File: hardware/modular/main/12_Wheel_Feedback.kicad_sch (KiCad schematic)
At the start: 6 parts, among them J6 ENCODER_8P, U28 TPS22919DCKR

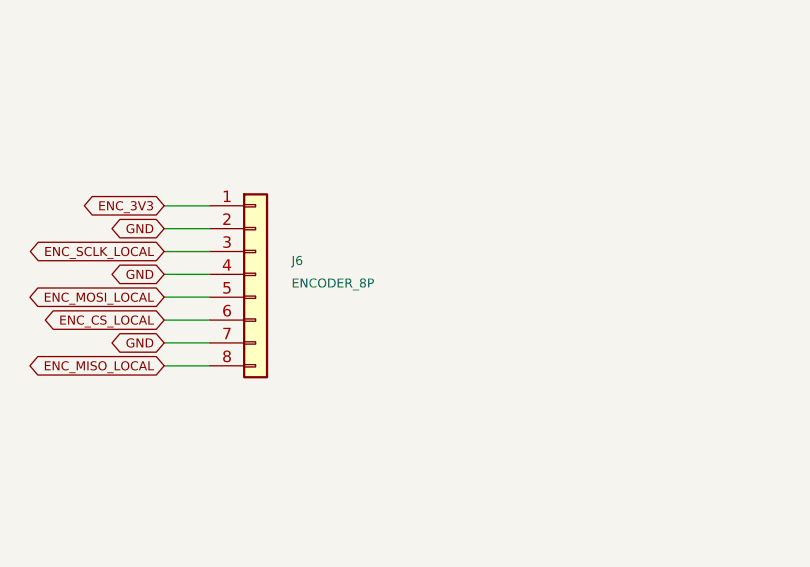
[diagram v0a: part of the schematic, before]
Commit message: Prepare wired Rev-A bench boards and submit manufacturing review
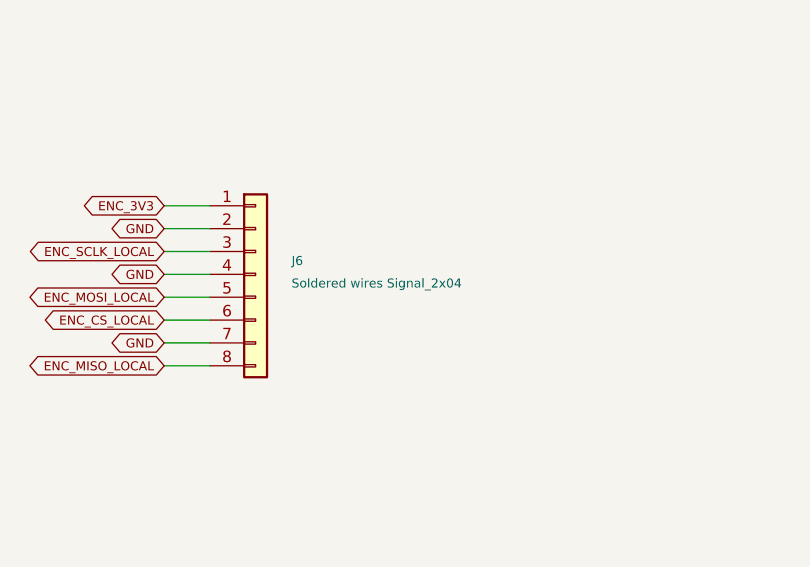
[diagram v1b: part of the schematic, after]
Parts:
- J6: value ENCODER_8P -> Soldered wires Signal_2x04; footprint Connector_JST:JST_SH_SM08B-SRSS-TB_1x08-1MP_P1.00mm_Horizontal -> MagMouseModular:Wire_Signal_2x04_P2.54mm; JLCPCB Part # C160407 -> (none); LCSC C160407 -> (none); MPN SM08B-SRSS-TB(LF)(SN) -> (none); Manufacturer JST -> (none); Sourcing Status JLCPCB SMT listing checked 2026-09-09; order stock and harn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 -> Hand-soldered wire termination; no connector fitted; do not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; Supplier URL https://www.lcsc.com/product-detail/C160407.html -> (none)
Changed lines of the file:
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@@
           (size 1.0 1.0))
         (justify left)))
-    (property "Value" "ENCODER_8P"
+    (property "Value" "Soldered wires Signal_2x04"
       (at 278.32 82.28 0)
       (effects
@@
           (size 1.0 1.0))
         (justify left)))
-    (property "Footprint" "Connector_JST:JST_SH_SM08B-SRSS-TB_1x08-1MP_P1.00mm_Horizontal"
+    (property "Footprint" "MagMouseModular:Wire_Signal_2x04_P2.54mm"
       (at 274.32 81.28 0)
       (hide yes)
@@
           (size 1.0 1.0))
         (justify left)))
-    (property "Datasheet" "https://www.jst-mfg.com/product/pdf/eng/eSH.pdf"
+    (property "Datasheet" ""
       (at 274.32 81.28 0)
       (hide yes)
@@
           (size 1.0 1.0))
         (justify left)))
-    (property "Manufacturer" "JST"
+    (property "Manufacturer" ""
       (at 274.32 81.28 0)
       (hide yes)
@@
           (size 1.0 1.0))
         (justify left)))
-    (property "MPN" "SM08B-SRSS-TB(LF)(SN)"
+    (property "MPN" ""
       (at 274.32 81.28 0)
       (hide yes)
@@
           (size 1.0 1.0))
         (justify left)))
-    (property "LCSC" "C160407"
+    (property "LCSC" ""
       (at 274.32 81.28 0)
       (hide yes)
@@
           (size 1.0 1.0))
         (justify left)))
-    (property "JLCPCB Part #" "C160407"
+    (property "JLCPCB Part #" ""
       (at 274.32 81.28 0)
       (hide yes)
@@
           (size 1.0 1.0))
         (justify left)))
-    (property "Sourcing Status" "JLCPCB SMT listing checked 2026-09-09; order stock and harness fit need confirmation"
+    (property "Sourcing Status" "Hand-soldered wire termination; no connector fitted; do not fill these holes"
       (at 274.32 81.28 0)
       (hide yes)
@@
           (size 1.0 1.0))
         (justify left)))
-    (property "Supplier URL" "https://www.lcsc.com/product-detail/C160407.html"
+    (property "Supplier URL" ""
       (at 274.32 81.28 0)
       (hide yes)
